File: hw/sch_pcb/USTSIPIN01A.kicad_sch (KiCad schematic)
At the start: 53 parts, among them M1 HOLE, M2 HOLE, M3 HOLE, M4 HOLE, M5 BMI-S-210-F, M6 BMI-S-210-F, M7 BMI-S-210-F, M8 BMI-S-204-F, U1 OPA2314, U2 OPA2314, U3 ISL21080DIH312Z-TK 1V25, U4 TS7211, U5 TS5A4594

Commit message: Edit schema
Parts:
- added C37: 1uF, Mlab_R:SMD-0805, symbol Device:C
- added Q1: (no value), symbol MLAB_T:Q_NJFET_SDG
- added R14, R16: 4k7, Mlab_R:SMD-0805, symbol Device:R
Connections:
- net A: now also Q1.3 (G)
- net GND: now also R14.2
- net K: now also C37.2, R16.1; no longer C24.1, R22.1
- net VCC1: now also Q1.2 (D)
- net +3V3 renamed POWER_ANALOG_3V3
- new net: C37.1, Q1.1 (S), R14.1
- new net Ubiasout: C24.1, R16.2, R22.1
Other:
- moved on the sheet: C1, C11, C12, C13, C14, C20, C4, C6, C7, C8, C9, R2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

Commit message: Edit schema
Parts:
- Q1: value (none) -> BF862; footprint (none) -> Mlab_T:SOT-23

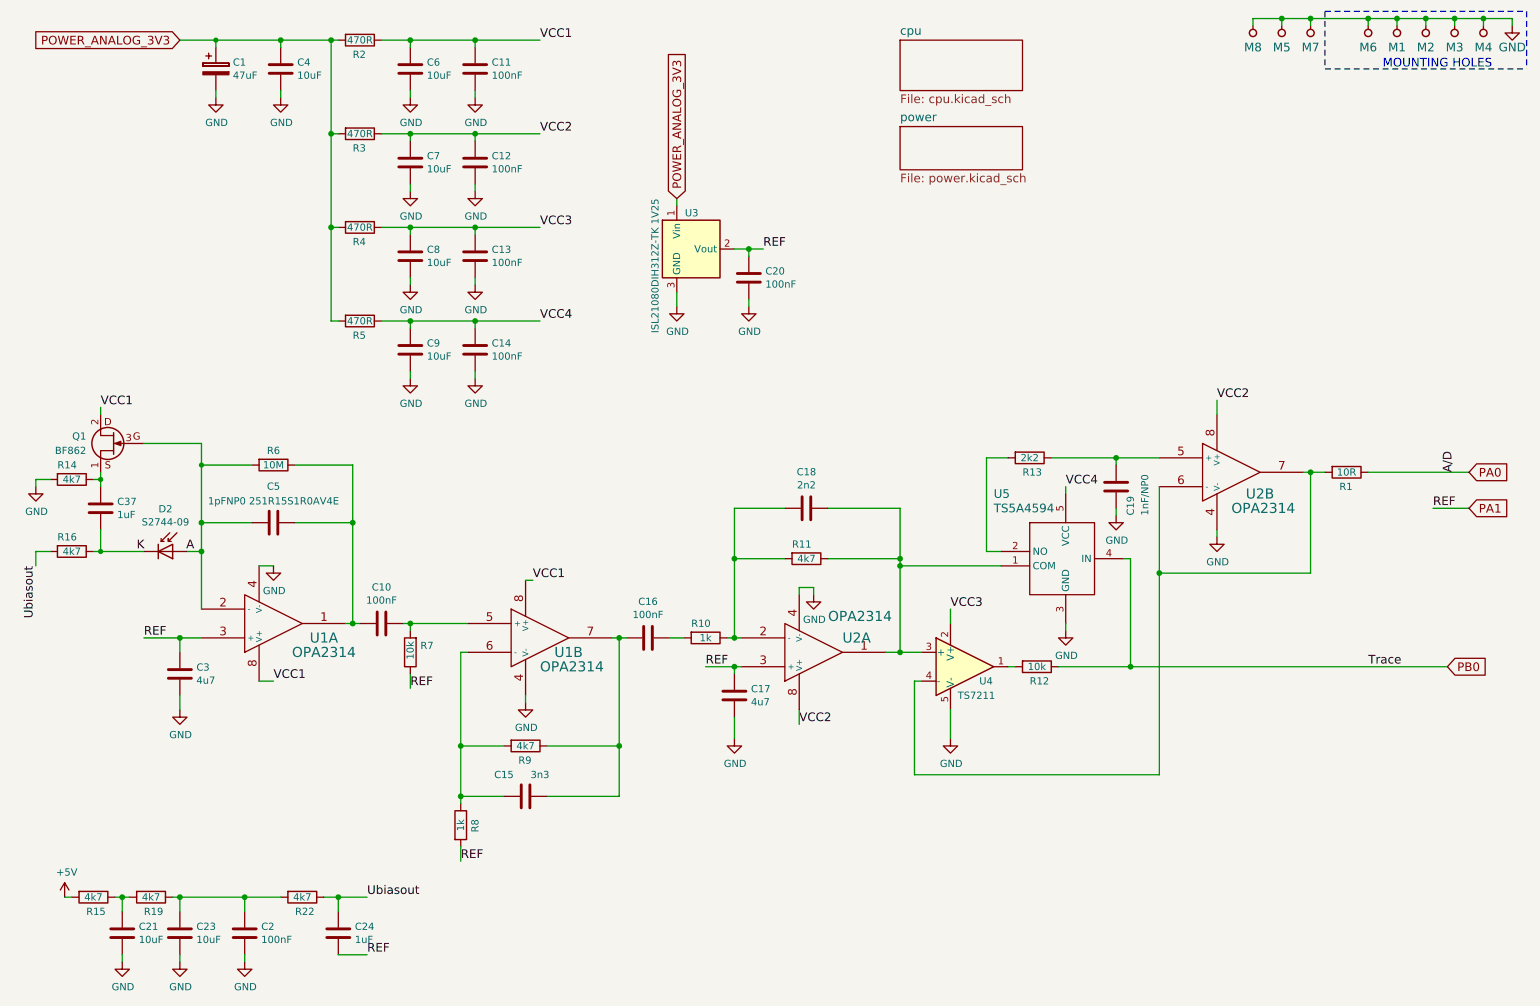
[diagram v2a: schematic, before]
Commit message: Edit schema and PCB
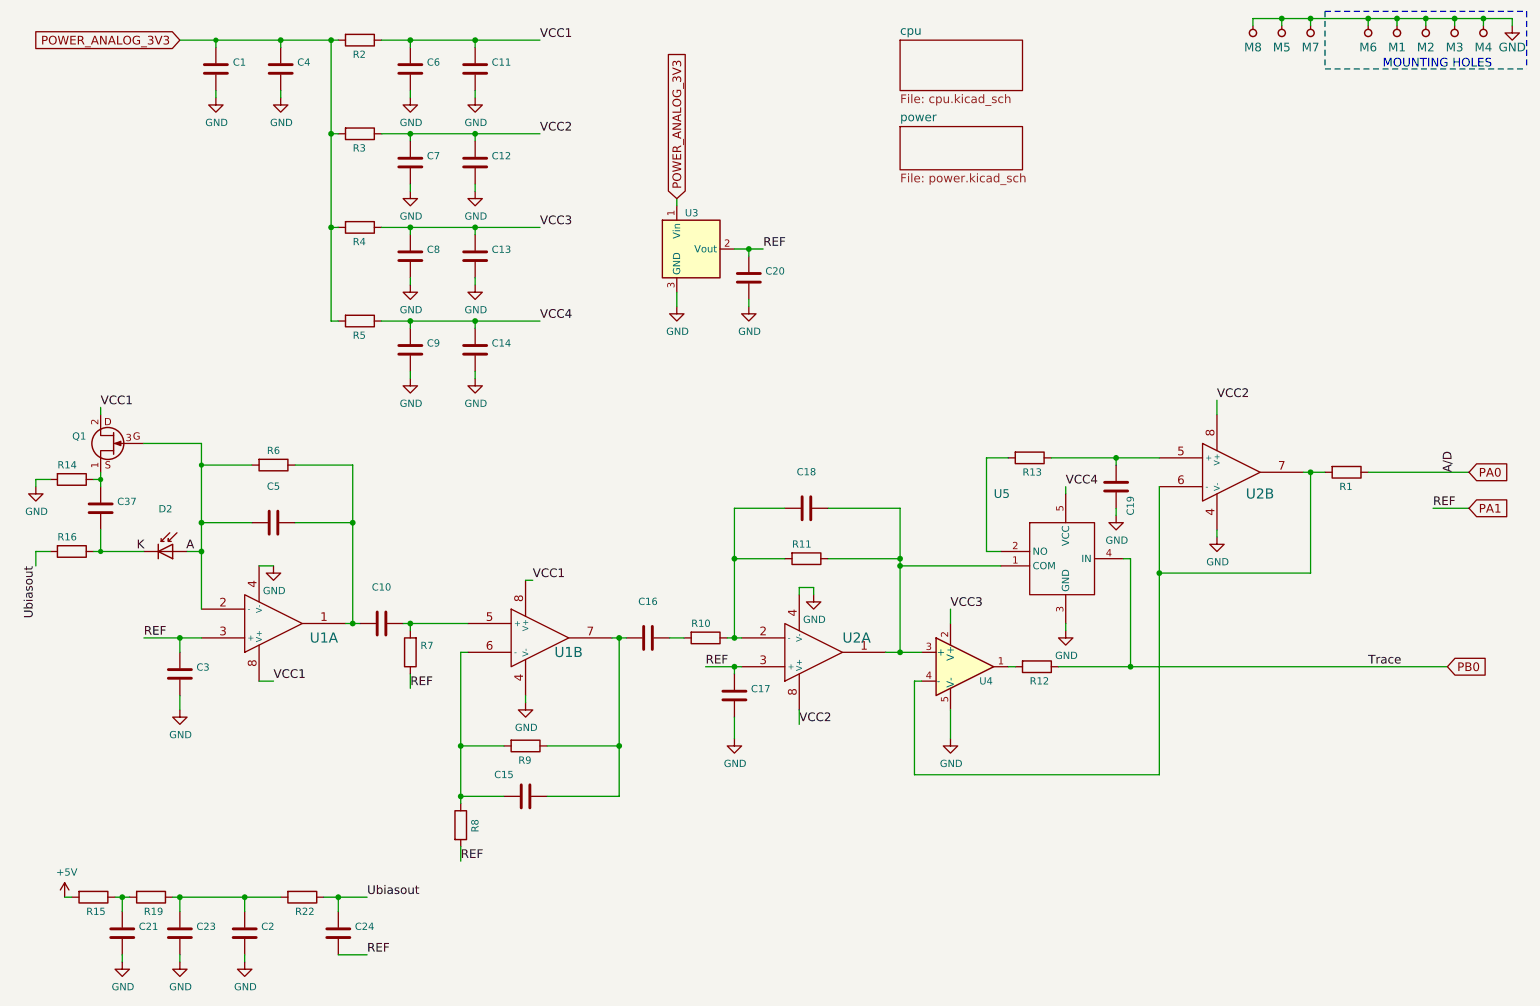
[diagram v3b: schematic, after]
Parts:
- C1: value 47uF -> (none); footprint Mlab_C:TantalC_SizeC_Reflow -> (none); symbol SPACEDOS01A_PCB01A-rescue:CP-Device -> Device:C; UST_ID 5c70984412875079b91f8867 -> 60d580ff1287500165f8595a
- C10, C11, C12, C13, C14, C16, C2, C20: value 100nF -> (none); footprint Mlab_R:SMD-0805 -> (none); UST_ID 5c70984712875079b91f8b4c -> (none)
- C15: value 3n3 -> (none); footprint Mlab_R:SMD-0805 -> (none); UST_ID 5c70984712875079b91f8b47 -> (none)
- C17, C3: value 4u7 -> (none); footprint Mlab_R:SMD-0805 -> (none); UST_ID 5c70984712875079b91f8b52 -> (none)
- C18: value 2n2 -> (none); footprint Mlab_R:SMD-0805 -> (none); UST_ID 5c70984712875079b91f8b46 -> (none)
- C19: value 1nF/NP0 -> (none); footprint Mlab_R:SMD-0805 -> (none); UST_ID 5c70984812875079b91f8ba6 -> (none)
- C21, C23, C4, C6, C7, C8, C9: value 10uF -> (none); footprint Mlab_R:SMD-0805 -> (none); UST_ID 5c70984812875079b91f8bbe -> (none)
- C24, C37: value 1uF -> (none); footprint Mlab_R:SMD-0805 -> (none); UST_ID 5c70984712875079b91f8b50 -> (none)
- C5: value 1pFNP0 251R15S1R0AV4E -> (none); footprint Mlab_R:SMD-0805 -> (none); UST_ID 5c70984712875079b91f8b9f -> (none)
- D2: value S2744-09 -> (none); footprint Mlab_D:HAMAMATSU_S2744-09 -> (none)
- M1, M2, M3, M4: value HOLE -> (none); footprint Mlab_Mechanical:MountingHole_3mm -> (none)
- M5, M6, M7: value BMI-S-210-F -> (none); footprint Mlab_Mechanical:BMI-S-210-F -> (none); UST_ID 5c70984312875079b91f873d -> (none)
- M8: value BMI-S-204-F -> (none); footprint RF_Shielding:Laird_Technologies_BMI-S-204-F_32.00x32.00mm -> (none); UST_ID 5c72751c1287500b4e11301a -> (none)
- Q1: value BF862 -> (none); footprint Mlab_T:SOT-23 -> (none)
- R1: value 10R -> (none); footprint Mlab_R:SMD-0805 -> (none); UST_ID 5c70984512875079b91f896d -> (none)
- R10, R8: value 1k -> (none); footprint Mlab_R:SMD-0805 -> (none); UST_ID 5c70984512875079b91f895c -> (none)
- R11, R14, R15, R16, R19, R22, R9: value 4k7 -> (none); footprint Mlab_R:SMD-0805 -> (none); UST_ID 5c70984612875079b91f8995 -> (none)
- R12, R7: value 10k -> (none); footprint Mlab_R:SMD-0805 -> (none); UST_ID 5c70984612875079b91f899f -> (none)
- R13: value 2k2 -> (none); footprint Mlab_R:SMD-0805 -> (none); UST_ID 5c70984612875079b91f8990 -> (none)
- R2, R3, R4, R5: value 470R -> (none); footprint Mlab_R:SMD-0805 -> (none); UST_ID 5c70984512875079b91f8986 -> (none)
- R6: value 10M -> (none); footprint Mlab_R:SMD-0805 -> (none); UST_ID 5c70984712875079b91f8aae -> (none)
- U1, U2: value OPA2314 -> (none); footprint Mlab_IO:SOIC-8_3.9x4.9mm_Pitch1.27mm -> (none); UST_ID 5c70984412875079b91f879b -> (none)
- U3: value ISL21080DIH312Z-TK 1V25 -> (none); footprint Package_TO_SOT_SMD:SOT-23 -> (none); UST_ID 5c70984712875079b91f8b7a -> (none)
- U4: value TS7211 -> (none); footprint Package_TO_SOT_SMD:SOT-23-5_HandSoldering -> (none); UST_ID 5c70984712875079b91f8b5b -> (none)
- U5: value TS5A4594 -> (none); footprint Package_TO_SOT_SMD:SOT-23-5_HandSoldering -> (none); UST_ID 5c70984612875079b91f8a0d -> (none)

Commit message: Edit schema and PCB
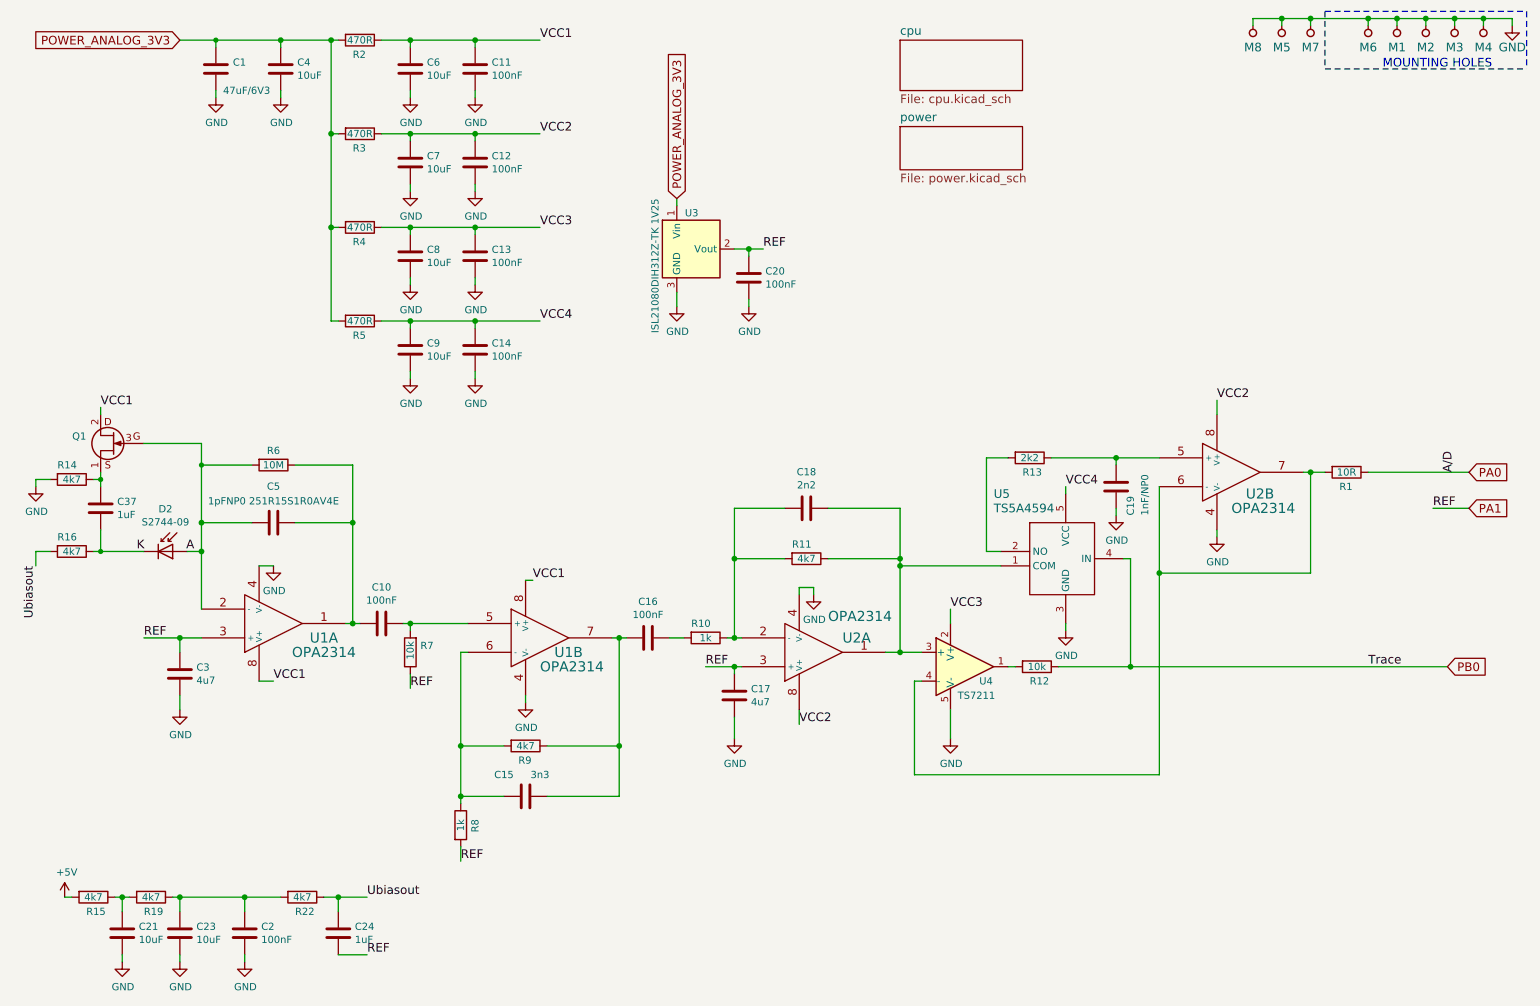
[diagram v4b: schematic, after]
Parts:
- C1: value (none) -> 47uF/6V3; footprint (none) -> Capacitor_SMD:C_0805_2012Metric
- C10, C11, C12, C13, C14, C16, C2, C20: value (none) -> 100nF; footprint (none) -> Capacitor_SMD:C_0603_1608Metric
- C15: value (none) -> 3n3; footprint (none) -> Capacitor_SMD:C_0603_1608Metric
- C17, C3: value (none) -> 4u7; footprint (none) -> Capacitor_SMD:C_0805_2012Metric
- C18: value (none) -> 2n2; footprint (none) -> Capacitor_SMD:C_0603_1608Metric
- C19: value (none) -> 1nF/NP0; footprint (none) -> Capacitor_SMD:C_0805_2012Metric
- C21, C23, C4, C6, C7, C8, C9: value (none) -> 10uF; footprint (none) -> Capacitor_SMD:C_0805_2012Metric
- C24, C37: value (none) -> 1uF; footprint (none) -> Capacitor_SMD:C_0603_1608Metric
- C5: value (none) -> 1pFNP0 251R15S1R0AV4E; footprint (none) -> Capacitor_SMD:C_0805_2012Metric
- D2: value (none) -> S2744-09; footprint (none) -> Mlab_D:HAMAMATSU_S2744-09
- M1, M2, M3, M4: value (none) -> HOLE; footprint (none) -> Mlab_Mechanical:MountingHole_3mm
- M5, M6, M7: value (none) -> BMI-S-210-F; footprint (none) -> Mlab_Mechanical:BMI-S-210-F
- M8: value (none) -> BMI-S-204-F; footprint (none) -> RF_Shielding:Laird_Technologies_BMI-S-204-F_32.00x32.00mm
- Q1: footprint (none) -> Package_TO_SOT_SMD:SOT-23
- R1: value (none) -> 10R; footprint (none) -> Resistor_SMD:R_0603_1608Metric
- R10, R8: value (none) -> 1k; footprint (none) -> Resistor_SMD:R_0603_1608Metric
- R11, R14, R15, R16, R19, R22, R9: value (none) -> 4k7; footprint (none) -> Resistor_SMD:R_0603_1608Metric
- R12, R7: value (none) -> 10k; footprint (none) -> Resistor_SMD:R_0603_1608Metric
- R13: value (none) -> 2k2; footprint (none) -> Resistor_SMD:R_0603_1608Metric
- R2, R3, R4, R5: value (none) -> 470R; footprint (none) -> Resistor_SMD:R_0603_1608Metric
- R6: value (none) -> 10M; footprint (none) -> Resistor_SMD:R_0603_1608Metric
- U1, U2: value (none) -> OPA2314; footprint (none) -> Package_SO:SOIC-8_3.9x4.9mm_P1.27mm
- U3: value (none) -> ISL21080DIH312Z-TK 1V25; footprint (none) -> Package_TO_SOT_SMD:SOT-23
- U4: value (none) -> TS7211; footprint (none) -> Package_TO_SOT_SMD:SOT-23-5_HandSoldering
- U5: value (none) -> TS5A4594; footprint (none) -> Package_TO_SOT_SMD:SOT-23-5_HandSoldering

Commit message: Edit
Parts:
- Q1: value (none) -> 2SK2394-6
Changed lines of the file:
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@@
     (pin "4")
     (pin "8")
+  )
+  (symbol (lib_id "MLAB_IO:AD8692") (at 156.21 128.27 0) (mirror x) (unit 1)
+    (in_bom yes) (on_board yes)
+    (property "Reference" "U2" (id 0) (at 161.29 125.73 0)
+      (effects (font (size 1.778 1.778)) (justify left))
+    )
+    (property "Value" "OPA2314" (id 1) (at 158.75 121.92 0)
+      (effects (font (size 1.778 1.778)) (justify left))
+    )
+    (property "Footprint" "Package_SO:SOIC-8_3.9x4.9mm_P1.27mm" (id 2) (at 156.21 128.27 0)
+      (effects (font (size 1.524 1.524)) hide)
+    )
+    (property "Datasheet" "" (id 3) (at 169.9514 125.1966 0)
+      (effects (font (size 1.524 1.524)) (justify left))
+    )
+    (property "UST_ID" "" (id 4) (at 156.21 128.27 0)
+      (effects (font (size 1.27 1.27)) hide)
+    )
+    (pin "1")
+    (pin "2")
+    (pin "3")
+    (pin "4")
+    (pin "8")
+  )
+  (symbol (lib_id "MLAB_IO:AD8692") (at 107.95 125.73 0) (unit 2)
+    (in_bom yes) (on_board yes)
+    (property "Reference" "U1" (id 0) (at 110.49 128.27 0)
+      (effects (font (size 1.778 1.778)) (justify left))
+    )
+    (property "Value" "OPA2314" (id 1) (at 107.95 130.81 0)
+      (effects (font (size 1.778 1.778)) (justify left))
+    )
+    (property "Footprint" "Package_SO:SOIC-8_3.9x4.9mm_P1.27mm" (id 2) (at 107.95 125.73 0)
+      (effects (font (size 1.524 1.524)) hide)
+    )
+    (property "Datasheet" "" (id 3) (at 121.6914 128.8034 0)
+      (effects (font (size 1.524 1.524)) (justify left))
+    )
+    (property "UST_ID" "" (id 4) (at 107.95 125.73 0)
+      (effects (font (size 1.27 1.27)) hide)
+    )
     (pin "4")
     (pin "5")
@@
     (pin "8")
   )
-  (symbol (lib_id "MLAB_IO:AD8692") (at 156.21 128.27 0) (mirror x) (unit 1)
-    (in_bom yes) (on_board yes)
-    (property "Reference" "U2" (id 0) (at 161.29 125.73 0)
+  (symbol (lib_id "MLAB_IO:AD8692") (at 229.87 96.52 0) (unit 2)
+    (in_bom yes) (on_board yes)
+    (property "Reference" "U2" (id 0) (at 232.41 100.33 0)
       (effects (font (size 1.778 1.778)) (justify left))
     )
-    (property "Value" "OPA2314" (id 1) (at 158.75 121.92 0)
+    (property "Value" "OPA2314" (id 1) (at 229.87 102.87 0)
       (effects (font (size 1.778 1.778)) (justify left))
     )
-    (property "Footprint" "Package_SO:SOIC-8_3.9x4.9mm_P1.27mm" (id 2) (at 156.21 128.27 0)
+    (property "Footprint" "Package_SO:SOIC-8_3.9x4.9mm_P1.27mm" (id 2) (at 229.87 96.52 0)
       (effects (font (size 1.524 1.524)) hide)
     )
-    (property "Datasheet" "" (id 3) (at 169.9514 125.1966 0)
+    (property "Datasheet" "" (id 3) (at 243.6114 99.5934 0)
       (effects (font (size 1.524 1.524)) (justify left))
     )
-    (property "UST_ID" "" (id 4) (at 156.21 128.27 0)
-      (effects (font (size 1.27 1.27)) hide)
-    )
-    (pin "1")
-    (pin "2")
-    (pin "3")
-    (pin "4")
-    (pin "8")
+    (property "UST_ID" "" (id 4) (at 229.87 96.52 0)
+      (effects (font (size 1.27 1.27)) hide)
+    )
     (pin "4")
     (pin "5")
@@
     (pin "8")
   )
-  (symbol (lib_id "MLAB_IO:AD8692") (at 107.95 125.73 0) (unit 2)
-    (in_bom yes) (on_board yes)
-    (property "Reference" "U1" (id 0) (at 110.49 128.27 0)
-      (effects (font (size 1.778 1.778)) (justify left))
-    )
-    (property "Value" "OPA2314" (id 1) (at 107.95 130.81 0)
-      (effects (font (size 1.778 1.778)) (justify left))
-    )
-    (property "Footprint" "Package_SO:SOIC-8_3.9x4.9mm_P1.27mm" (id 2) (at 107.95 125.73 0)
-      (effects (font (size 1.524 1.524)) hide)
-    )
-    (property "Datasheet" "" (id 3) (at 121.6914 128.8034 0)
-      (effects (font (size 1.524 1.524)) (justify left))
-    )
-    (property "UST_ID" "" (id 4) (at 107.95 125.73 0)
-      (effects (font (size 1.27 1.27)) hide)
-    )
-    (pin "1")
-    (pin "2")
-    (pin "3")
-    (pin "4")
-    (pin "8")
-    (pin "4")
-    (pin "5")
-    (pin "6")
-    (pin "7")
-    (pin "8")
-  )
-  (symbol (lib_id "MLAB_IO:AD8692") (at 229.87 96.52 0) (unit 2)
-    (in_bom yes) (on_board yes)
-    (property "Reference" "U2" (id 0) (at 232.41 100.33 0)
-      (effects (font (size 1.778 1.778)) (justify left))
-    )
-    (property "Value" "OPA2314" (id 1) (at 229.87 102.87 0)
-      (effects (font (size 1.778 1.778)) (justify left))
-    )
-    (property "Footprint" "Package_SO:SOIC-8_3.9x4.9mm_P1.27mm" (id 2) (at 229.87 96.52 0)
-      (effects (font (size 1.524 1.524)) hide)
-    )
-    (property "Datasheet" "" (id 3) (at 243.6114 99.5934 0)
-      (effects (font (size 1.524 1.524)) (justify left))
-    )
-    (property "UST_ID" "" (id 4) (at 229.87 96.52 0)
-      (effects (font (size 1.27 1.27)) hide)
-    )
-    (pin "1")
-    (pin "2")
-    (pin "3")
-    (pin "4")
-    (pin "8")
-    (pin "4")
-    (pin "5")
-    (pin "6")
-    (pin "7")
-    (pin "8")
-  )
   (symbol (lib_id "Device:C") (at 44.45 132.08 0) (unit 1)
     (in_bom yes) (on_board yes)
@@
       (effects (font (size 1.27 1.27)) (justify left))
     )
-    (property "Value" "" (id 1) (at 27.94 92.7098 0)
+    (property "Value" "2SK2394-6" (id 1) (at 27.94 92.7098 0)
       (effects (font (size 1.27 1.27)) (justify left))
     )
@@
       (reference "#PWR044") (unit 1) (value "GND") (footprint "")
     )
-    (path "/00000000-0000-0000-0000-00005c69bcb4/93528073-c0cb-4183-a6d8-18d260ff8463"
-      (reference "#PWR046") (unit 1) (value "+5V") (footprint "")
-    )
-    (path "/00000000-0000-0000-0000-00005c69bcb4/91d14c97-5067-46dc-833d-758c3007da2a"
-      (reference "#PWR047") (unit 1) (value "+5V") (footprint "")
-    )
     (path "/00000000-0000-0000-0000-00005b3dc120"
       (reference "#PWR0101") (unit 1) (value "GND") (footprint "")
@@
       (reference "#PWR0171") (unit 1) (value "GND") (footprint "")
     )
+    (path "/00000000-0000-0000-0000-00005c69bcb4/adb76a2a-bf68-4549-b705-c85f6ebc67ff"
+      (reference "#PWR?") (unit 1) (value "+3.3V") (footprint "")
+    )
+    (path "/00000000-0000-0000-0000-00005c69bcb4/bbe736ba-72b3-4b0f-8f28-b8b9a7812b71"
+      (reference "#PWR?") (unit 1) (value "+3.3V") (footprint "")
+    )
     (path "/00000000-0000-0000-0000-00005b46ae4b"
       (reference "C1") (unit 1) (value "47uF/6V3") (footprint "Capacitor_SMD:C_0805_2012Metric")
@@
       (reference "R31") (unit 1) (value "5k1") (footprint "Resistor_SMD:R_0603_1608Metric")
     )
+    (path "/00000000-0000-0000-0000-00005c4aedd8/3e2cc6d6-d223-4ebd-82bf-5723d1fd76b8"
+      (reference "R?") (unit 1) (value "100") (footprint "Resistor_SMD:R_0603_1608Metric")
+    )
+    (path "/00000000-0000-0000-0000-00005c4aedd8/a8b4ea89-6f58-45df-bee1-0c71b5c38ff1"
+      (reference "R?") (unit 1) (value "100") (footprint "Resistor_SMD:R_0603_1608Metric")
+    )
     (path "/00000000-0000-0000-0000-00005b39c1e6"
